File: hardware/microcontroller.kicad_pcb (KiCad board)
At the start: 2 copper layers, 50.8 x 78.7 mm, 72 parts, among them J5 1x2 jumper right-angle, J6 RJ45_Amphenol_RJMG1BD3B8K1ANR, J7 1x2 jumper right-angle, U1 W5500, U10 register file, U11 register file, U12 3.3V <=> 5V, U13 flip-flop, U14 3.3V <=> 5V, U16 3.3V <=> 5V, U17 decoder, U3 counter, U4 counter, U5 counter, U6 counter, U7 counter, U8 shift register, U9 shift register, Y1 25MHz

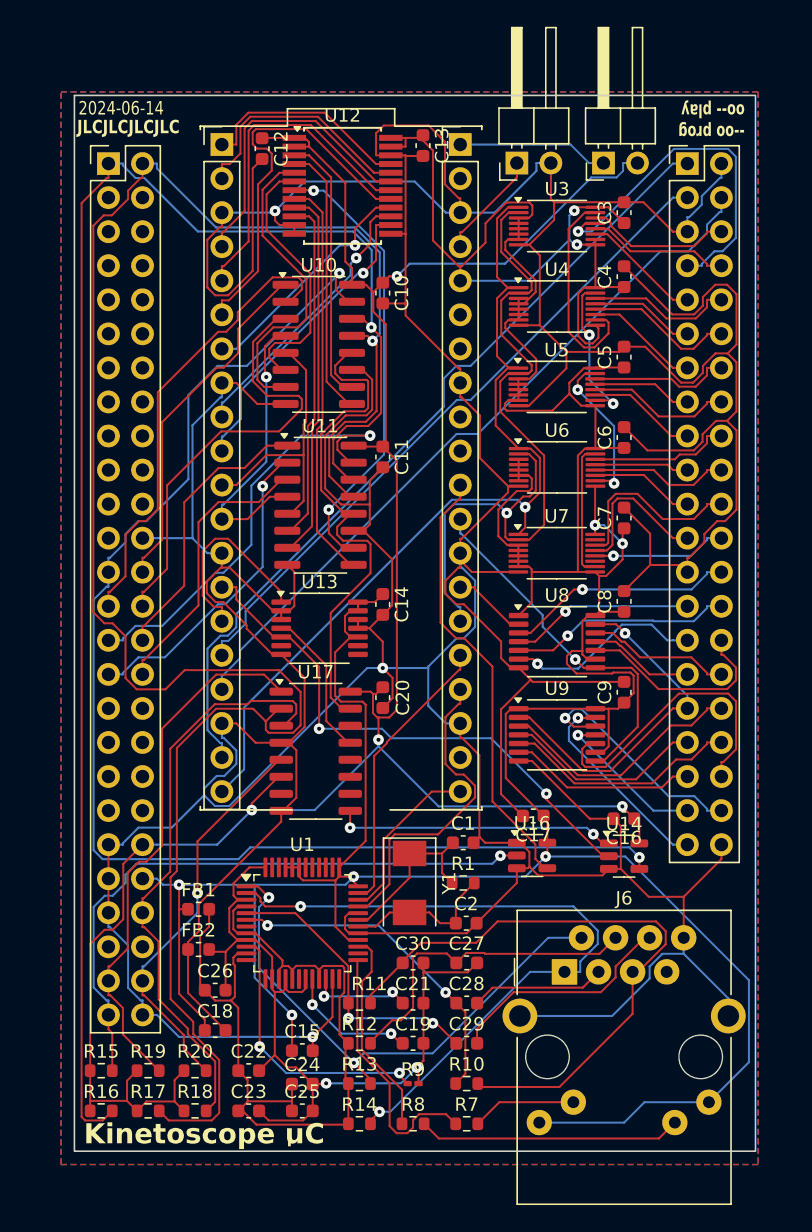
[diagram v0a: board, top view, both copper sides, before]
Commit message: Fix ethernet chip-select and register address decoder
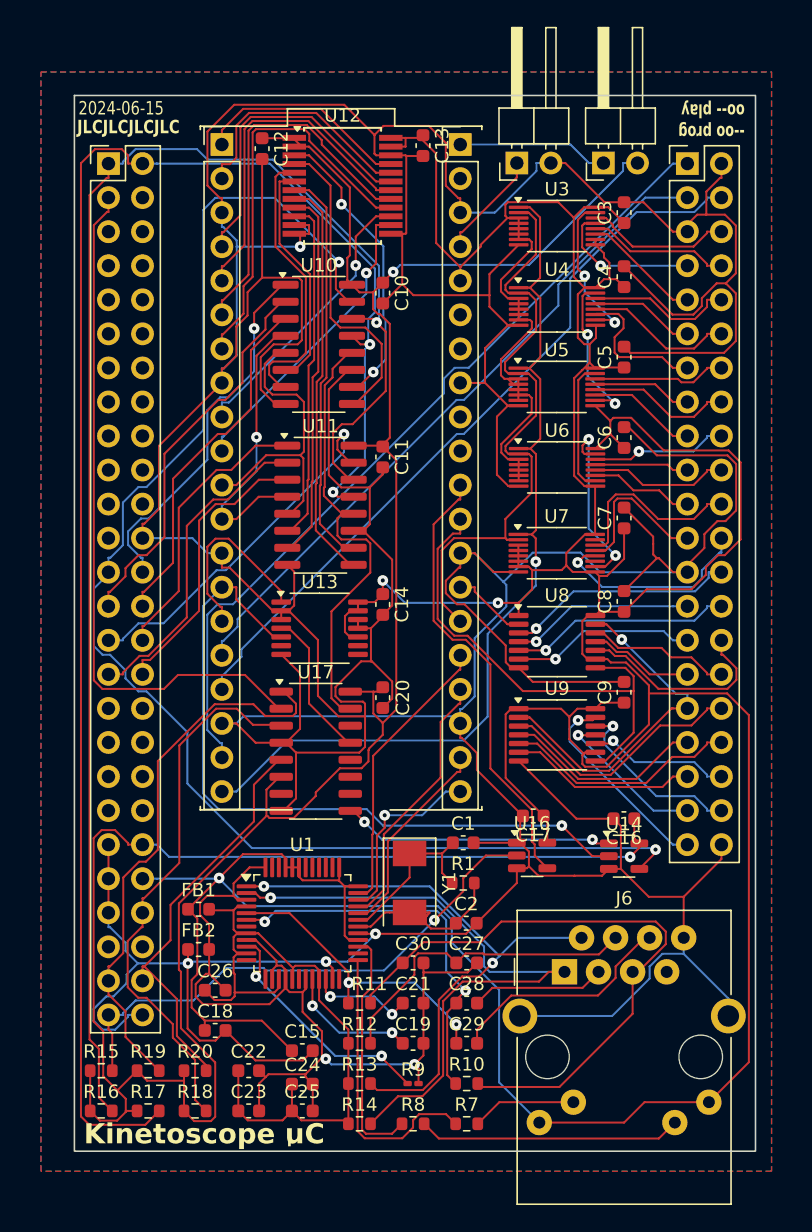
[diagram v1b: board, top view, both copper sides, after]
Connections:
- J4 pad 19: unconnected-(J4-GP17-Pad19) -> /~{SPI_CS}
- U1 pad 32: GND -> /~{SPI_CS}
- U17 pad 2: /kinetoscope-header-internal/SEGA_A2 -> /kinetoscope-header-internal/SEGA_A3
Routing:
- net /kinetoscope-header-internal/SEGA_A3: track 0.00 -> 52.2 mm
- net +5V: track 167.6 -> 210.4 mm, vias 4 -> 2
- net +3.3V: track 323.7 -> 354.2 mm, vias 8 -> 3
- net /kinetoscope-header-internal/SEGA_A2: track 150.3 -> 125.4 mm, vias 1 -> 2
- net /address-counter-internal/A2: track 26.7 -> 11.1 mm
- net /~{SPI_CS}: track 0.00 -> 15.3 mm
- net /SYNC_3V: track 40.7 -> 54.7 mm, vias 2 -> 1
- net /REG_R_D5: track 17.7 -> 30.3 mm, vias 1 -> 0
- net /data-register-internal/D12: track 22.5 -> 10.7 mm, vias 0 -> 1
- net +3.3VA: track 63.5 -> 52.0 mm
- net /SRAM_W_A_CLK: track 56.8 -> 46.3 mm, vias 1 -> 0
- net /SRAM_D_CLK: track 27.3 -> 36.4 mm, vias 1 -> 0
- net GNDA: track 62.2 -> 71.1 mm
- net /SEGA_D0: track 97.8 -> 105.2 mm
- net /SEGA_D3: track 33.3 -> 26.4 mm
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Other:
- board text added: "2024-06-15"
- board text removed: "2024-06-14"

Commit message: Add second sync bit to flag errors back to the Sega
Also split firmware speed tests out into their own file
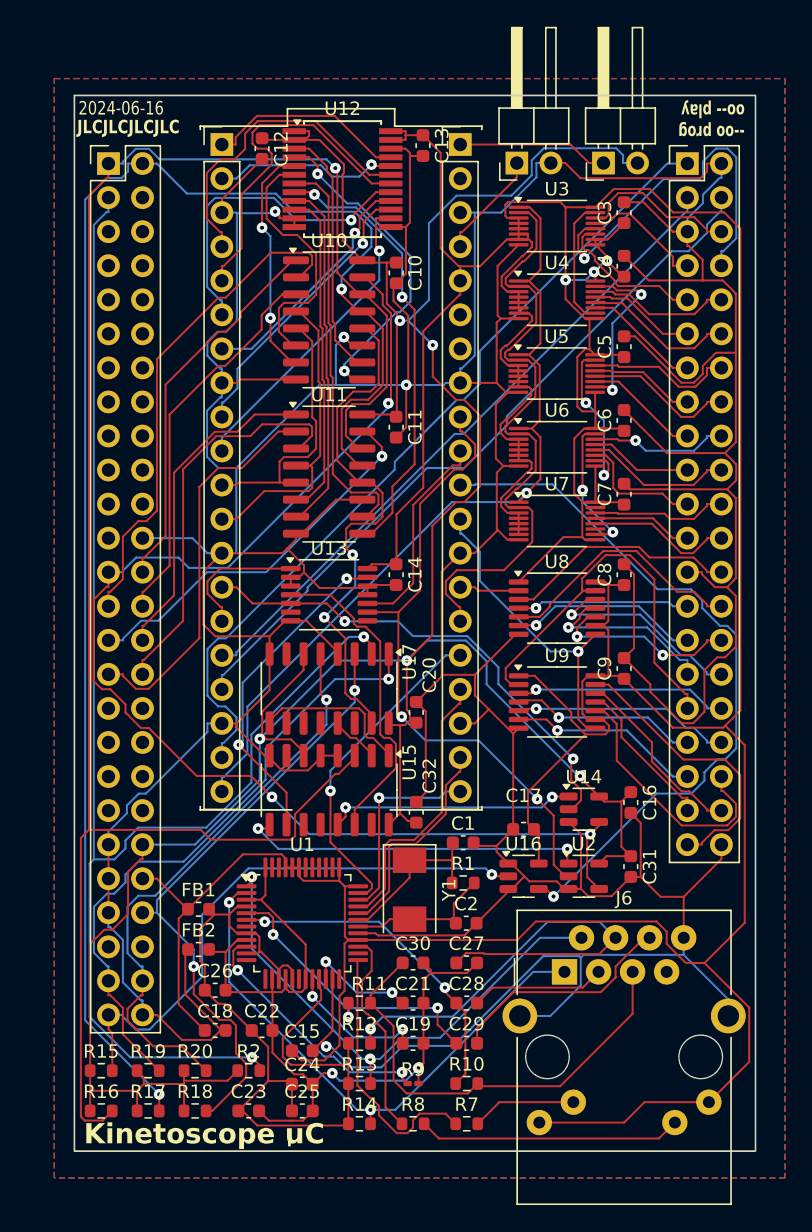
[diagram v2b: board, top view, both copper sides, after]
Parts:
- added C31: 22nF, Capacitor_SMD:C_0603_1608Metric, F.Cu at (60.2, 76.8)
- added C32: 22nF, Capacitor_SMD:C_0603_1608Metric, F.Cu at (44.2, 72.8)
- added R2: 10k, Resistor_SMD:R_0603_1608Metric, F.Cu at (31.7, 92.0)
- added U15: decoder, Package_SO:SO-16_3.9x9.9mm_P1.27mm, F.Cu at (37.7, 71.1)
- added U2: 3.3V <=> 5V, Package_TO_SOT_SMD:SOT-23-5, F.Cu at (56.7, 77.5)
- moved U17 4.78 mm to (37.7, 63.5), turned to -90 degrees
- moved U14 4.61 mm to (56.7, 72.5)
- moved C22 3.16 mm to (32.7, 89.0)
- moved C20 2.73 mm to (44.2, 65.3), turned to 90 degrees
- moved U13 2.60 mm to (37.7, 56.5)
- moved U8 2.50 mm to (54.7, 57.5)
- moved U9 2.45 mm to (54.7, 64.5)
- moved C11 2.44 mm to (42.7, 44.0)
- moved C14 2.44 mm to (42.7, 55.0)
- moved U11 2.41 mm to (37.7, 47.5)
- moved U7 2.40 mm to (54.7, 51.0)
- moved C8 2.00 mm to (59.7, 55.0)
- moved U10 1.98 mm to (37.7, 36.0)
- moved C10 1.80 mm to (42.7, 32.5)
- moved C7 1.77 mm to (59.7, 49.0)
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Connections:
- net /SYNC_3V renamed /CMD_3V
- net /~{SYNC_CLR} renamed /~{CMD_CLR}
- J4 pad 10: unconnected-(J4-GP26/A0-Pad10) -> /~{ERR_SET}
- J4 pad 9: unconnected-(J4-GP27/A1-Pad9) -> /ERR_3V
- U13 pad 10: +3.3V -> /~{ERR_SET}
- U13 pad 13: +3.3V -> /~{ERR_CLR}
- U13 pad 4: /~{SYNC_SET} -> /~{CMD_SET}
- U13 pad 9: unconnected-(U13B-Q-Pad9) -> /ERR_3V
- U14 pad 1: /~{SYNC_OE} -> /~{CMD_OE}
- U17 pad 13: /~{SYNC_SET} -> /~{SYNC_WE}
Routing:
- net /kinetoscope-header-internal/SEGA_A3: track 52.2 -> 107.3 mm, vias 0 -> 2
- net /ERR_3V: track 0.00 -> 47.6 mm, vias 0 -> 2
- net GND: track 561.9 -> 535.2 mm
- net /~{ERR_OE}: track 0.00 -> 25.8 mm, vias 0 -> 2
- net /~{ERR_CLR}: track 0.00 -> 24.8 mm, vias 0 -> 2
- net /kinetoscope-header-internal/SEGA_A1: track 117.5 -> 142.1 mm
- net /~{CMD_SET}: track 0.00 -> 24.0 mm
- net /~{RESET_3V}: track 33.6 -> 54.0 mm, vias 0 -> 1
- net /~{CMD_OE}: track 0.00 -> 18.5 mm, vias 0 -> 2
- net +3.3V: track 354.2 -> 372.1 mm
- net /CMD_3V: track 54.7 -> 36.9 mm, vias 1 -> 2
- net /address-counter-internal/A3: track 10.6 -> 27.7 mm, vias 0 -> 1
- net /~{ERR_SET}: track 0.00 -> 15.7 mm
- net /SRAM_D_CLK: track 36.4 -> 23.2 mm, vias 0 -> 1
- net /~{SEGA_AS}: track 30.6 -> 42.9 mm, vias 0 -> 1
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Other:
- board text added: "2024-06-16"
- board text removed: "2024-06-15"

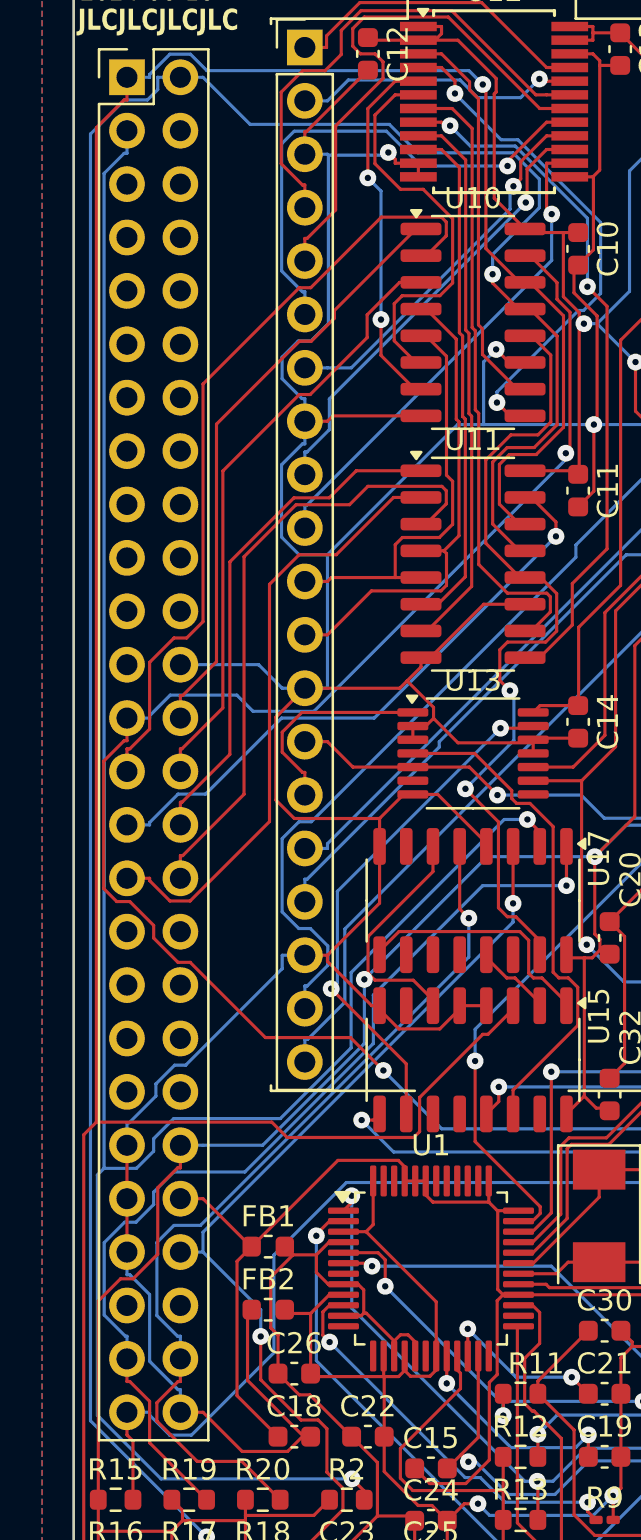
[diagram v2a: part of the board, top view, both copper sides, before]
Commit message: Update interboard header in microcontroller and SRAM boards
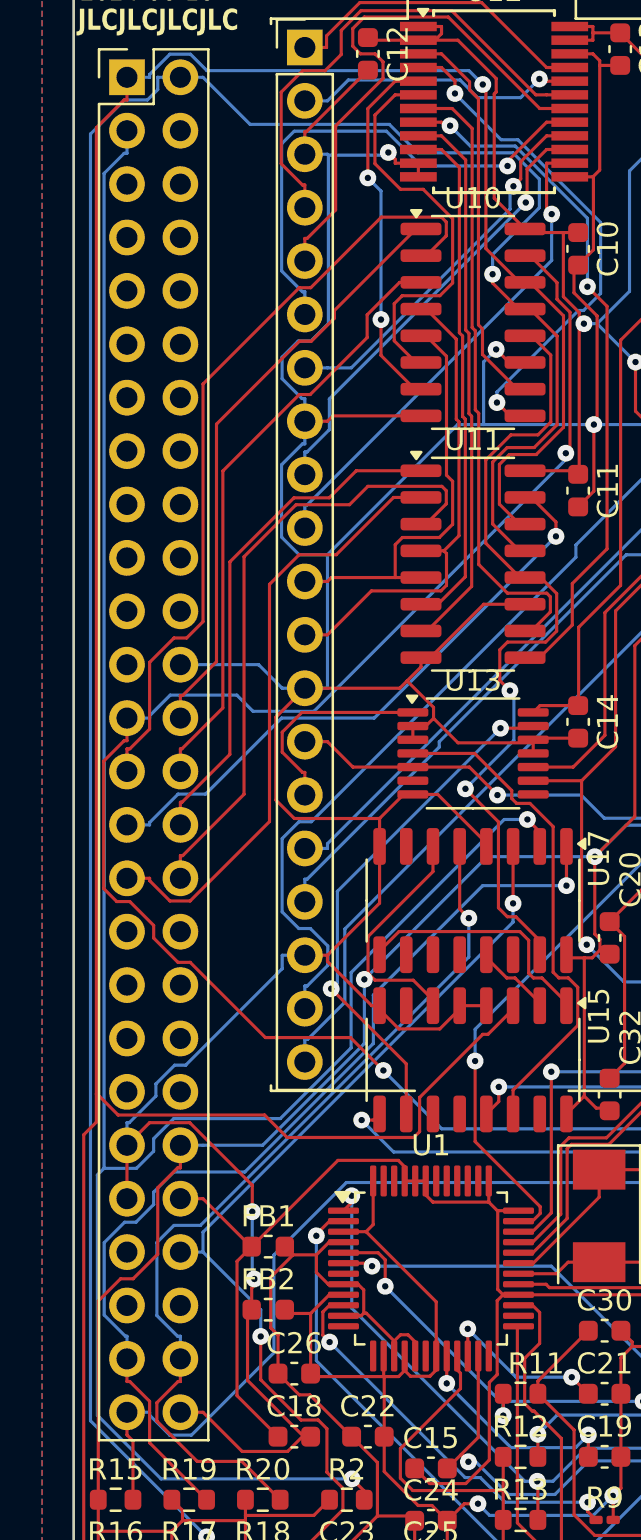
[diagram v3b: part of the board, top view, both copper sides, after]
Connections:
- J1 pad 45: GND -> /kinetoscope-header-internal/~{SEGA_OE}
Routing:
- net GND: track 535.2 -> 537.5 mm, vias 4 -> 6
- net /kinetoscope-header-internal/SEGA_A1: track 142.1 -> 142.6 mm
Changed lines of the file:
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@@
 	(net 178 "unconnected-(U15-Y7-Pad7)")
 	(net 179 "/ERR_3V")
+	(net 180 "/kinetoscope-header-internal/~{SEGA_OE}")
 	(footprint "Capacitor_SMD:C_0603_1608Metric"
 		(layer "F.Cu")
@@
 			(net 66 "/SEGA_D0")
 			(pinfunction "Y")
-			(pintype "output")
+			(pintype "tri_state")
 		)
 		(pad "5" smd roundrect
@@
 			(layers "*.Cu" "*.Mask")
 			(remove_unused_layers no)
-			(net 132 "GND")
-			(pinfunction "GND")
-			(pintype "passive")
+			(net 180 "/kinetoscope-header-internal/~{SEGA_OE}")
+			(pinfunction "~{SEGA_OE}")
+			(pintype "passive+no_connect")
 		)
 		(pad "46" thru_hole oval
@@
 			(net 66 "/SEGA_D0")
 			(pinfunction "Y")
-			(pintype "output")
+			(pintype "tri_state")
 		)
 		(pad "5" smd roundrect
@@
 	)
 	(segment
+		(start 35.2 74.5314)
+		(end 34.923 74.8084)
+		(width 0.15)
+		(layer "F.Cu")
+		(net 6)
+	)
+	(segment
+		(start 19.8239 26.7782)
+		(end 19.8239 72.74)
+		(width 0.15)
+		(layer "F.Cu")
+		(net 6)
+	)
+	(segment
 		(start 39.4678 42.3246)
 		(end 38.9947 42.7977)
@@
 	)
 	(segment
-		(start 28.8963 74.8084)
-		(end 34.923 74.8084)
+		(start 38.2036 69.9019)
+		(end 35.2 72.9055)
 		(width 0.15)
 		(layer "F.Cu")
@@
 	)
 	(segment
-		(start 21.565 95.04)
-		(end 20.8452 95.7598)
+		(start 20.85972 73.74)
+		(end 19.85972 72.74)
 		(width 0.15)
 		(layer "F.Cu")
@@
 	)
 	(segment
-		(start 35.2 74.5314)
-		(end 35.2 72.9055)
+		(start 21.565 95.04)
+		(end 20.8452 95.7598)
 		(width 0.15)
 		(layer "F.Cu")
@@
 	)
 	(segment
-		(start 34.923 74.8084)
-		(end 35.2 74.5314)
+		(start 19.8239 72.74)
+		(end 19.8239 74.0784)
 		(width 0.15)
 		(layer "F.Cu")
@@
 	)
 	(segment
-		(start 19.8239 26.7782)
-		(end 19.8239 74.0784)
+		(start 39.645 68.7104)
+		(end 38.4535 69.9019)
 		(width 0.15)
 		(layer "F.Cu")
@@
 	)
 	(segment
-		(start 38.9947 44.6825)
-		(end 39.9472 45.635)
+		(start 19.85972 72.74)
+		(end 19.8239 72.74)
 		(width 0.15)
 		(layer "F.Cu")
@@
 	)
 	(segment
-		(start 21.28 24.38)
-		(end 21.28 25.4567)
+		(start 27.8279 73.74)
+		(end 20.85972 73.74)
 		(width 0.15)
 		(layer "F.Cu")
@@
 	)
 	(segment
-		(start 40.215 34.135)
-		(end 40.4536 34.135)
+		(start 38.9947 44.6825)
+		(end 39.9472 45.635)
 		(width 0.15)
 		(layer "F.Cu")
@@
 	)
 	(segment
-		(start 39.645 68.7104)
-		(end 39.645 68.54)
+		(start 39.645 68.54)
+		(end 39.645 68.7104)
 		(width 0.15)
 		(layer "F.Cu")
@@
 	)
 	(segment
-		(start 19.8239 74.0784)
-		(end 28.1663 74.0784)
+		(start 21.28 24.38)
+		(end 21.28 25.4567)
 		(width 0.15)
 		(layer "F.Cu")
@@
 	)
 	(segment
-		(start 19.5023 95.7598)
-		(end 19.2232 95.4807)
+		(start 40.215 34.135)
+		(end 40.4536 34.135)
 		(width 0.15)
 		(layer "F.Cu")
@@
 	)
 	(segment
-		(start 28.1663 74.0784)
-		(end 28.8963 74.8084)
+		(start 28.8963 74.8084)
+		(end 27.8279 73.74)
 		(width 0.15)
 		(layer "F.Cu")
@@
 	)
 	(segment
-		(start 19.2232 95.4807)
-		(end 19.2232 74.6791)
+		(start 19.5023 95.7598)
+		(end 19.2232 95.4807)
 		(width 0.15)
 		(layer "F.Cu")
@@
 	)
 	(segment
-		(start 42.0434 35.7248)
-		(end 42.0434 41.0276)
+		(start 19.2232 95.4807)
+		(end 19.2232 74.6791)
 		(width 0.15)
 		(layer "F.Cu")
@@
 	)
 	(segment
-		(start 38.2036 69.9019)
-		(end 38.4535 69.9019)
+		(start 42.0434 35.7248)
+		(end 42.0434 41.0276)
 		(width 0.15)
 		(layer "F.Cu")
@@
 	)
 	(segment
-		(start 38.4535 69.9019)
-		(end 39.645 68.7104)
+		(start 35.2 72.9055)
+		(end 35.2 74.5314)
 		(width 0.15)
 		(layer "F.Cu")
@@
 	)
 	(segment
-		(start 35.2 72.9055)
-		(end 38.2036 69.9019)
+		(start 34.923 74.8084)
+		(end 28.8963 74.8084)
 		(width 0.15)
 		(layer "F.Cu")
@@
 	)
 	(segment
+		(start 38.4535 69.9019)
+		(end 38.2036 69.9019)
+		(width 0.15)
+		(layer "F.Cu")
+		(net 6)
+	)
+	(segment
 		(start 38.3528 32.5272)
 		(end 38.3528 24.87)
@@
 	)
 	(segment
+		(start 27.34 81.84)
+		(end 27.2125 81.9675)
+		(width 0.15)
+		(layer "F.Cu")
+		(net 132)
+	)
+	(segment
 		(start 39.9025 81.79)
 		(end 41.2125 81.79)
@@
 	)
 	(segment
+		(start 27.24 77.07972)
+		(end 27.24 78.34)
+		(width 0.15)
+		(layer "F.Cu")
+		(net 132)
+	)
+	(segment
 		(start 56.4878 25.4711)
 		(end 65.436 25.4711)
@@
 	)
 	(segment
+		(start 27.2125 81.9675)
+		(end 27.2125 83)
+		(width 0.15)
+		(layer "F.Cu")
+		(net 132)
+	)
+	(segment
 		(start 34.4406 58.49)
 		(end 34.8775 58.49)
@@
 	)
 	(segment
+		(start 27.34 81.54)
+		(end 27.34 81.84)
+		(width 0.15)
+		(layer "F.Cu")
+		(net 132)
+	)
+	(segment
 		(start 56.5265 78.49)
 		(end 55.6025 78.49)
@@
 	)
 	(segment
+		(start 21.28 75.18)
+		(end 22.355 74.105)
+		(width 0.15)
+		(layer "F.Cu")
+		(net 132)
+	)
+	(segment
 		(start 28.361 54.819)
 		(end 29.74 53.44)
@@
 	)
 	(segment
-		(start 21.28 77.72)
-		(end 21.28 80.26)
-		(width 0.15)
-		(layer "F.Cu")
-		(net 132)
-	)
-	(segment
 		(start 29.2402 59.6356)
 		(end 28.361 58.7564)
@@
 	)
 	(segment
+		(start 24.26528 74.105)
+		(end 27.24 77.07972)
+		(width 0.15)
+		(layer "F.Cu")
+		(net 132)
+	)
+	(segment
 		(start 44.9489 65.2489)
 		(end 44.9489 71.2811)
@@
 		(net 132)
 	)
+	(segment
+		(start 22.355 74.105)
+		(end 24.26528 74.105)
+		(width 0.15)
+		(layer "F.Cu")
+		(net 132)
+	)
 	(via
 		(at 37.5191 90.2355)
@@
 	)
 	(via
+		(at 27.24 78.34)
+		(size 0.8)
+		(drill 0.3)
+		(layers "F.Cu" "B.Cu")
+		(net 132)
+	)
+	(via
+		(at 27.34 81.54)
+		(size 0.8)
+		(drill 0.3)
+		(layers "F.Cu" "B.Cu")
+		(net 132)
+	)
+	(via
 		(at 33.7115 27.9563)
 		(size 0.8)
@@
 	)
 	(segment
-		(start 21.28 80.26)
-		(end 21.28 81.3367)
-		(width 0.15)
-		(layer "B.Cu")
-		(net 132)
-	)
-	(segment
 		(start 67 25.4567)
 		(end 66.8653 25.4567)
@@
 	)
 	(segment
-		(start 21.28 81.3367)
-		(end 21.4147 81.3367)
-		(width 0.15)
-		(layer "B.Cu")
-		(net 132)
-	)
-	(segment
 		(start 29.4205 36.93)
 		(end 28.6579 37.6926)
@@
 	)
 	(segment
-		(start 23.82 87.88)
-		(end 23.82 86.8033)
-		(width 0.15)
-		(layer "B.Cu")
-		(net 132)
-	)
-	(segment
 		(start 56.3783 83.4933)
 		(end 53.7147 83.4933)
@@
 	)
 	(segment
-		(start 21.4147 81.3367)
-		(end 22.3567 82.2787)
-		(width 0.15)
-		(layer "B.Cu")
-		(net 132)
-	)
-	(segment
 		(start 38.2427 40.8975)
 		(end 38.2427 37.9209)
@@
 	)
 	(segment
-		(start 23.7084 86.8033)
-		(end 23.82 86.8033)
-		(width 0.15)
-		(layer "B.Cu")
-		(net 132)
-	)
-	(segment
-		(start 22.3567 82.2787)
-		(end 22.3567 85.4516)
-		(width 0.15)
-		(layer "B.Cu")
-		(net 132)
-	)
-	(segment
 		(start 29.4726 47.09)
 		(end 28.6329 46.2503)
@@
 	)
 	(segment
-		(start 22.3567 85.4516)
-		(end 23.7084 86.8033)
-		(width 0.15)
-		(layer "B.Cu")
-		(net 132)
-	)
-	(segment
 		(start 56.7244 83.4)
 		(end 56.5047 83.6197)
@@
 	)
 	(segment
+		(start 27.24 81.44)
+		(end 27.34 81.54)
+		(width 0.15)
+		(layer "B.Cu")
+		(net 132)
+	)
+	(segment
 		(start 46.2858 40.8975)
 		(end 46.4433 40.74)
@@
 		(width 0.15)
 		(layer "B.Cu")
+		(net 132)
+	)
+	(segment
+		(start 27.24 78.34)
+		(end 27.24 81.44)
+		(width 0.15)
+		(layer "B.Cu")
